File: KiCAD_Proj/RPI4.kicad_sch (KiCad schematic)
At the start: 1 part, among them U3 RASPBERRY_PI_4B_4GB

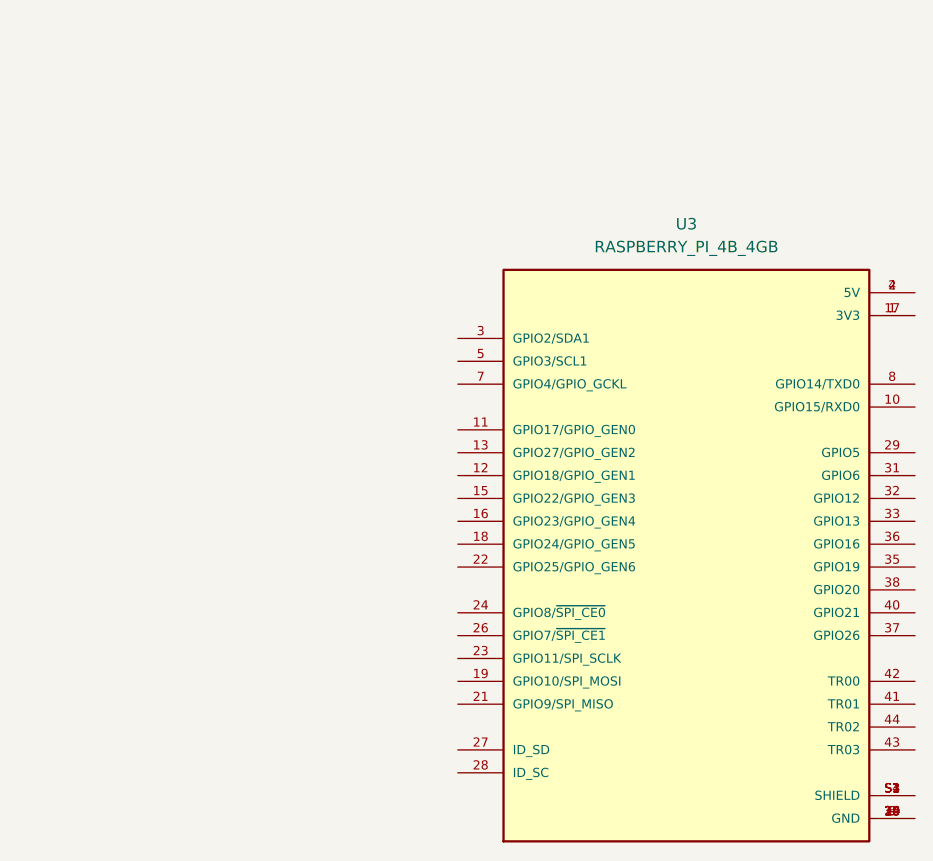
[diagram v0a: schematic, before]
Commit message: Added Pi HAT reference footprint
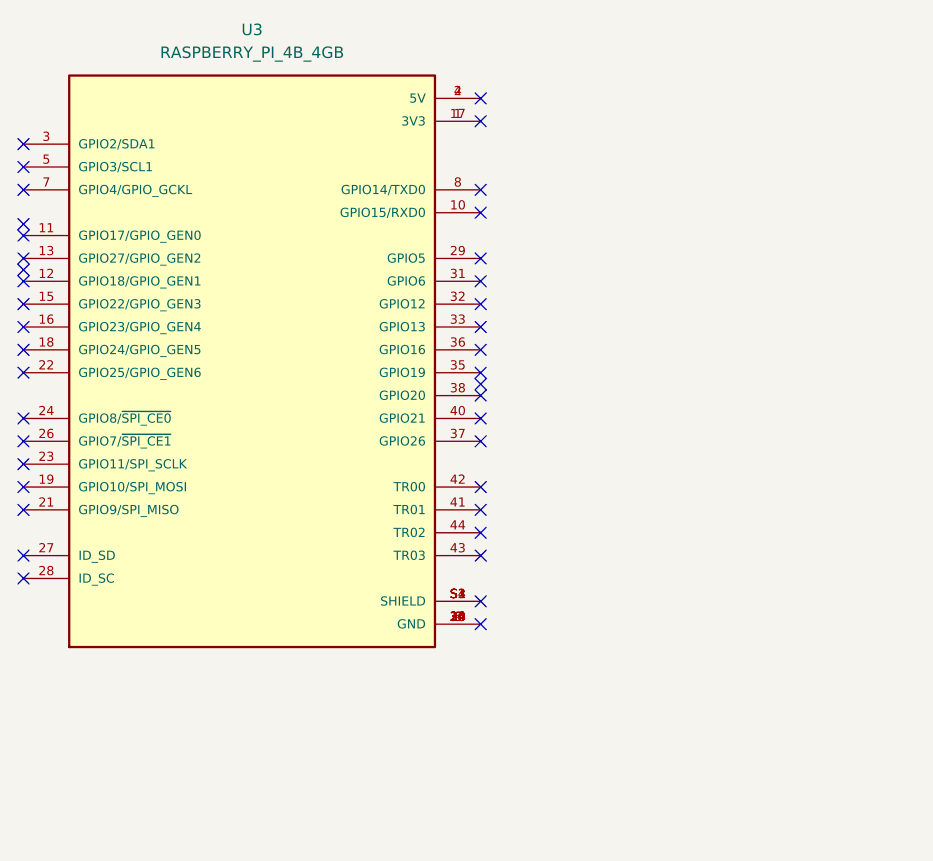
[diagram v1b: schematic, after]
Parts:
- U3: footprint RASPBERRY_PI_4B_4GB:MODULE_RASPBERRY_PI_4B_4GB -> Healthbot-Footprints:MODULE_RASPBERRY_PI_4B_4GB
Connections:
- no-connect marks 0 -> 39
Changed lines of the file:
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@@
 	(generator_version "8.0")
 	(paper "A4")
+	(no_connect
+		(at 77.47 55.88)
+	)
+	(no_connect
+		(at 26.67 48.26)
+	)
+	(no_connect
+		(at 77.47 53.34)
+	)
+	(no_connect
+		(at 26.67 71.12)
+	)
+	(no_connect
+		(at 77.47 62.23)
+	)
+	(no_connect
+		(at 77.47 68.58)
+	)
+	(no_connect
+		(at 77.47 40.64)
+	)
+	(no_connect
+		(at 77.47 50.8)
+	)
+	(no_connect
+		(at 26.67 83.82)
+	)
+	(no_connect
+		(at 77.47 81.28)
+	)
+	(no_connect
+		(at 26.67 66.04)
+	)
+	(no_connect
+		(at 26.67 38.1)
+	)
+	(no_connect
+		(at 77.47 86.36)
+	)
+	(no_connect
+		(at 77.47 66.04)
+	)
+	(no_connect
+		(at 77.47 63.5)
+	)
+	(no_connect
+		(at 26.67 68.58)
+	)
+	(no_connect
+		(at 26.67 81.28)
+	)
+	(no_connect
+		(at 26.67 53.34)
+	)
+	(no_connect
+		(at 77.47 76.2)
+	)
+	(no_connect
+		(at 77.47 78.74)
+	)
+	(no_connect
+		(at 77.47 60.96)
+	)
+	(no_connect
+		(at 26.67 49.53)
+	)
+	(no_connect
+		(at 77.47 48.26)
+	)
+	(no_connect
+		(at 26.67 50.8)
+	)
+	(no_connect
+		(at 26.67 58.42)
+	)
+	(no_connect
+		(at 26.67 35.56)
+	)
+	(no_connect
+		(at 77.47 33.02)
+	)
+	(no_connect
+		(at 26.67 76.2)
+	)
+	(no_connect
+		(at 77.47 73.66)
+	)
+	(no_connect
+		(at 26.67 55.88)
+	)
+	(no_connect
+		(at 26.67 40.64)
+	)
+	(no_connect
+		(at 26.67 60.96)
+	)
+	(no_connect
+		(at 26.67 44.45)
+	)
+	(no_connect
+		(at 77.47 88.9)
+	)
+	(no_connect
+		(at 26.67 73.66)
+	)
+	(no_connect
+		(at 77.47 30.48)
+	)
+	(no_connect
+		(at 77.47 58.42)
+	)
+	(no_connect
+		(at 77.47 43.18)
+	)
+	(no_connect
+		(at 26.67 45.72)
+	)
 	(symbol
 		(lib_id "Healthbot-Symbols:RASPBERRY_PI_4B_4GB")
-		(at 100.33 82.55 0)
+		(at 52.07 60.96 0)
 		(unit 1)
 		(exclude_from_sim no)
@@
 		(fields_autoplaced yes)
 		(property "Reference" "U3"
-			(at 100.33 44.45 0)
+			(at 52.07 22.86 0)
 			(effects
 				(font
@@
 		)
 		(property "Value" "RASPBERRY_PI_4B_4GB"
-			(at 100.33 46.99 0)
-			(effects
-				(font
-					(size 1.27 1.27)
-				)
-			)
-		)
-		(property "Footprint" "RASPBERRY_PI_4B_4GB:MODULE_RASPBERRY_PI_4B_4GB"
-			(at 100.33 82.55 0)
+			(at 52.07 25.4 0)
+			(effects
+				(font
+					(size 1.27 1.27)
+				)
+			)
+		)
+		(property "Footprint" "Healthbot-Footprints:MODULE_RASPBERRY_PI_4B_4GB"
+			(at 52.07 60.96 0)
 			(effects
 				(font
@@
 		)
 		(property "Datasheet" ""
-			(at 100.33 82.55 0)
+			(at 52.07 60.96 0)
 			(effects
 				(font
@@
 		)
 		(property "Description" ""
-			(at 100.33 82.55 0)
+			(at 52.07 60.96 0)
 			(effects
 				(font
@@
 		)
 		(property "MF" "Raspberry Pi"
-			(at 100.33 82.55 0)
+			(at 52.07 60.96 0)
 			(effects
 				(font
@@
 		)
 		(property "MAXIMUM_PACKAGE_HEIGHT" "16 mm"
-			(at 100.33 82.55 0)
+			(at 52.07 60.96 0)
 			(effects
 				(font
@@
 		)
 		(property "Package" "None"
-			(at 100.33 82.55 0)
+			(at 52.07 60.96 0)
 			(effects
 				(font
@@
 		)
 		(property "Price" "None"
-			(at 100.33 82.55 0)
+			(at 52.07 60.96 0)
 			(effects
 				(font
@@
 		)
 		(property "Check_prices" "https://www.snapeda.com/parts/RASPBERRY%20PI%204B/4GB/Raspberry+Pi/view-part/?ref=eda"
-			(at 100.33 82.55 0)
+			(at 52.07 60.96 0)
 			(effects
 				(font
@@
 		)
 		(property "STANDARD" "Manufacturer Recommendations"
-			(at 100.33 82.55 0)
+			(at 52.07 60.96 0)
 			(effects
 				(font
@@
 		)
 		(property "PARTREV" "4"
-			(at 100.33 82.55 0)
+			(at 52.07 60.96 0)
 			(effects
 				(font
@@
 		)
 		(property "SnapEDA_Link" "https://www.snapeda.com/parts/RASPBERRY%20PI%204B/4GB/Raspberry+Pi/view-part/?ref=snap"
-			(at 100.33 82.55 0)
+			(at 52.07 60.96 0)
 			(effects
 				(font
@@
 		)
 		(property "MP" "RASPBERRY PI 4B/4GB"
-			(at 100.33 82.55 0)
+			(at 52.07 60.96 0)
 			(effects
 				(font
@@
 		)
 		(property "Description_1" "\nBCM2711 Raspberry Pi 4 Model B 4GB - ARM® Cortex®-A72 MPU Embedded Evaluation Board\n"
-			(at 100.33 82.55 0)
+			(at 52.07 60.96 0)
 			(effects
 				(font
@@
 		)
 		(property "MANUFACTURER" "Raspberry Pi"
-			(at 100.33 82.55 0)
+			(at 52.07 60.96 0)
 			(effects
 				(font
@@
 		)
 		(property "Availability" "In Stock"
-			(at 100.33 82.55 0)
+			(at 52.07 60.96 0)
 			(effects
 				(font
@@
 		)
 		(property "SNAPEDA_PN" "RASPBERRY PI 4B/4GB"
-			(at 100.33 82.55 0)
-			(effects
-				(font
-					(size 1.27 1.27)
-				)
-				(justify bottom)
-				(hide yes)
-			)
+			(at 52.07 60.96 0)
+			(effects
+				(font
+					(size 1.27 1.27)
+				)
+				(justify bottom)
+				(hide yes)
+			)
+		)
+		(pin "4"
+		)
+		(pin "11"
+		)
+		(pin "21"
+		)
+		(pin "9"
+		)
+		(pin "19"
+		)
+		(pin "6"
+		)
+		(pin "S2"
+		)
+		(pin "27"
+		)
+		(pin "22"
+		)
+		(pin "8"
+		)
+		(pin "34"
+		)
+		(pin "43"
+		)
+		(pin "10"
+		)
+		(pin "18"
+		)
+		(pin "41"
+		)
+		(pin "17"
+		)
+		(pin "7"
+		)
+		(pin "25"
+		)
+		(pin "42"
+		)
+		(pin "32"
+		)
+		(pin "S3"
+		)
+		(pin "S4"
+		)
+		(pin "15"
+		)
+		(pin "38"
+		)
+		(pin "30"
+		)
+		(pin "14"
+		)
+		(pin "16"
+		)
+		(pin "36"
+		)
+		(pin "39"
+		)
+		(pin "13"
+		)
+		(pin "26"
+		)
+		(pin "28"
 		)
 		(pin "31"
 		)
-		(pin "13"
-		)
 		(pin "20"
 		)
-		(pin "25"
-		)
-		(pin "32"
-		)
-		(pin "21"
-		)
-		(pin "10"
-		)
-		(pin "15"
-		)
-		(pin "18"
+		(pin "3"
+		)
+		(pin "40"
+		)
+		(pin "5"
+		)
+		(pin "37"
+		)
+		(pin "2"
+		)
+		(pin "23"
 		)
 		(pin "24"
 		)
-		(pin "38"
-		)
-		(pin "S3"
-		)
-		(pin "39"
-		)
-		(pin "6"
-		)
-		(pin "7"
-		)
-		(pin "8"
-		)
-		(pin "43"
-		)
-		(pin "22"
-		)
-		(pin "34"
-		)
-		(pin "16"
-		)
-		(pin "19"
-		)
-		(pin "40"
-		)
-		(pin "5"
-		)
-		(pin "17"
-		)
 		(pin "12"
 		)
-		(pin "14"
-		)
-		(pin "26"
-		)
-		(pin "27"
+		(pin "35"
+		)
+		(pin "33"
+		)
+		(pin "44"
+		)
+		(pin "S1"
 		)
 		(pin "29"
 		)
-		(pin "30"
-		)
 		(pin "1"
-		)
-		(pin "3"
-		)
-		(pin "33"
-		)
-		(pin "35"
-		)
-		(pin "23"
-		)
-		(pin "36"
-		)
-		(pin "2"
-		)
-		(pin "41"
-		)
-		(pin "28"
-		)
-		(pin "42"
-		)
-		(pin "S1"
-		)
-		(pin "S2"
-		)
-		(pin "11"
-		)
-		(pin "4"
-		)
-		(pin "S4"
-		)
-		(pin "44"
-		)
-		(pin "37"
-		)
-		(pin "9"
 		)
 		(instances
 			(project "universalConnectorBoard"
-				(path "/4d36baa7-ef48-416a-b1c8-6a662c0af28f/278048b1-6074-4239-8c06-afc2cf6cbf8a"
+				(path "/4d36baa7-ef48-416a-b1c8-6a662c0af28f/81ebf2d6-63ef-43f9-ac0a-87a453d7d172"
 					(reference "U3")
 					(unit 1)
